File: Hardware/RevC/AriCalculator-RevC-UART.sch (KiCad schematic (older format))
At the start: 15 parts, among them CON3 USB-MINI-B, IC4 FT232RL

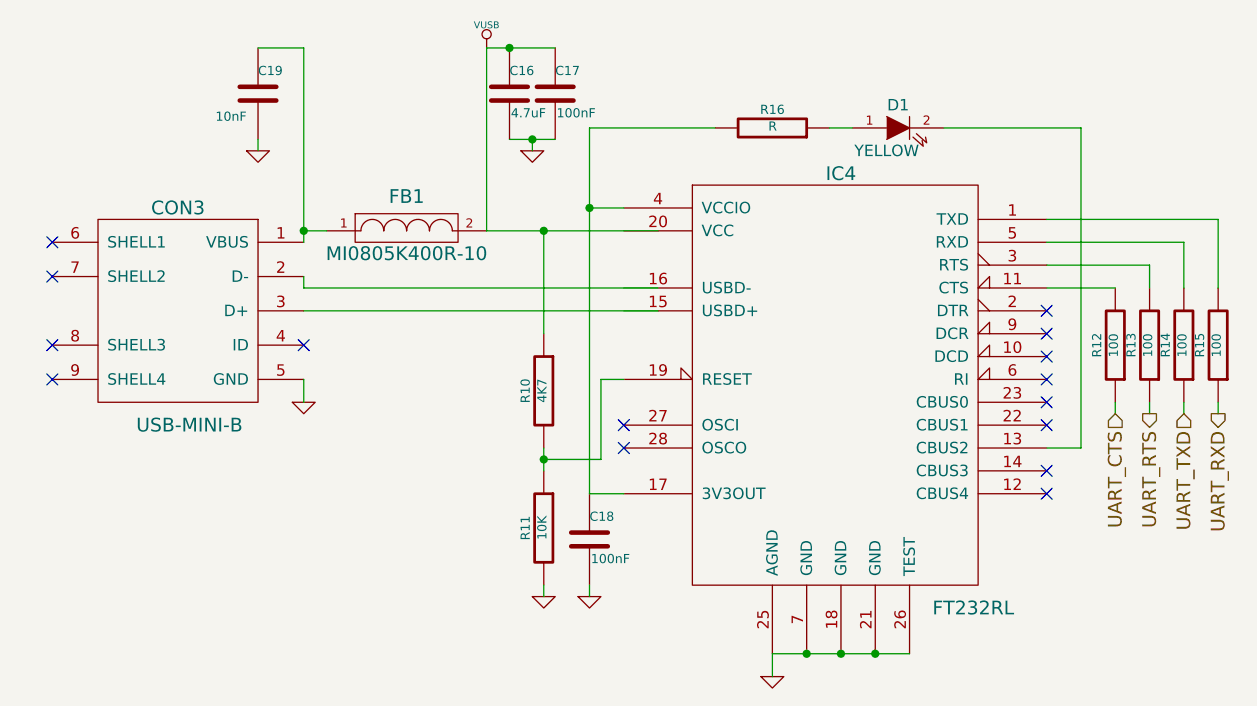
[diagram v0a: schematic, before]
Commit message: cleaned up schematic
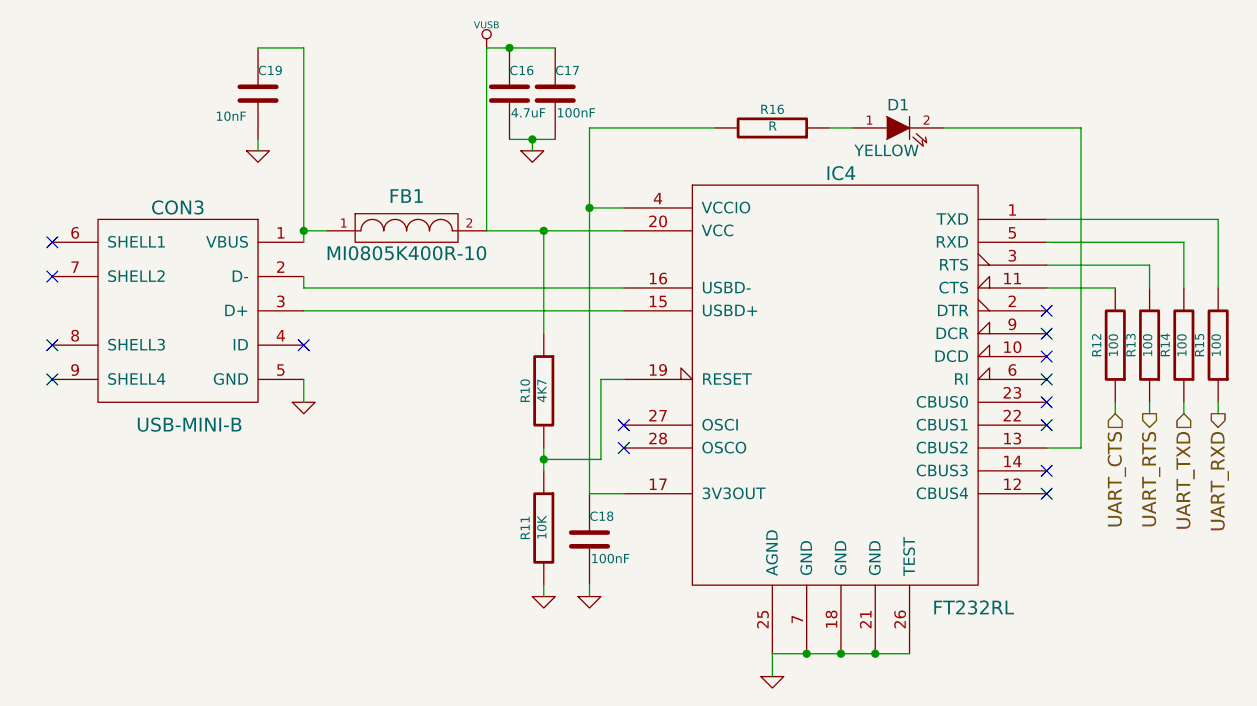
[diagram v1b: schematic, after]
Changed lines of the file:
@@
 	3650 2900 3650 3000
 Wire Wire Line
-	3400 1950 4150 1950
+	3400 1950 4000 1950
 Wire Wire Line
 	3650 1950 3650 2400
 Connection ~ 3650 2950
 Wire Wire Line
-	4150 2300 2600 2300
+	4000 2300 2600 2300
 Wire Wire Line
-	4150 2200 2600 2200
+	4000 2200 2600 2200
 Wire Wire Line
 	3850 1500 3850 3100

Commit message: work in progress
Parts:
- R16: value R -> 120
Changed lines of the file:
@@
 EESchema Schematic File Version 2
-LIBS:power
-LIBS:device
-LIBS:transistors
-LIBS:conn
-LIBS:linear
-LIBS:regul
-LIBS:74xx
-LIBS:cmos4000
-LIBS:adc-dac
-LIBS:memory
-LIBS:xilinx
-LIBS:special
-LIBS:microcontrollers
-LIBS:dsp
-LIBS:microchip
-LIBS:analog_switches
-LIBS:motorola
-LIBS:texas
-LIBS:intel
-LIBS:audio
-LIBS:interface
-LIBS:digital-audio
-LIBS:philips
-LIBS:display
-LIBS:cypress
-LIBS:siliconi
-LIBS:opto
-LIBS:atmel
-LIBS:contrib
-LIBS:valves
-LIBS:w_microcontrollers
 LIBS:AriCalculator
-LIBS:w_analog
-LIBS:w_connectors
-LIBS:w_device
-LIBS:AriCalculator-RevC-Main-cache
+LIBS:AriCalculator-RevC-cache
 EELAYER 27 0
 EELAYER END
@@
 Sheet 5 6
 Title "UART"
-Date "29 oct 2014"
+Date "3 nov 2014"
 Rev "RevC"
 Comp "Dirk Heisswolf"
@@
 P 4650 1500
 F 0 "R16" V 4730 1500 40  0000 C CNN
-F 1 "R" V 4657 1501 40  0000 C CNN
+F 1 "120" V 4657 1501 40  0000 C CNN
 F 2 "~" V 4580 1500 30  0000 C CNN
 F 3 "~" H 4650 1500 30  0000 C CNN

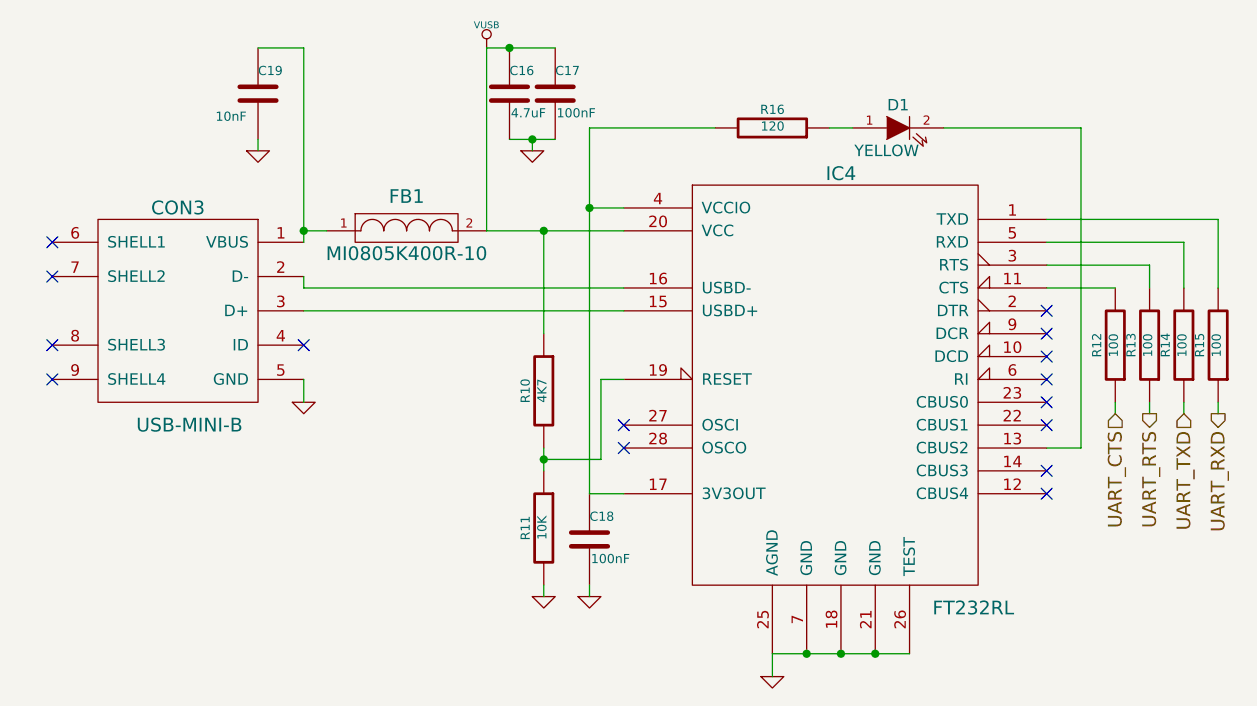
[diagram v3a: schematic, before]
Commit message: started RevC layout
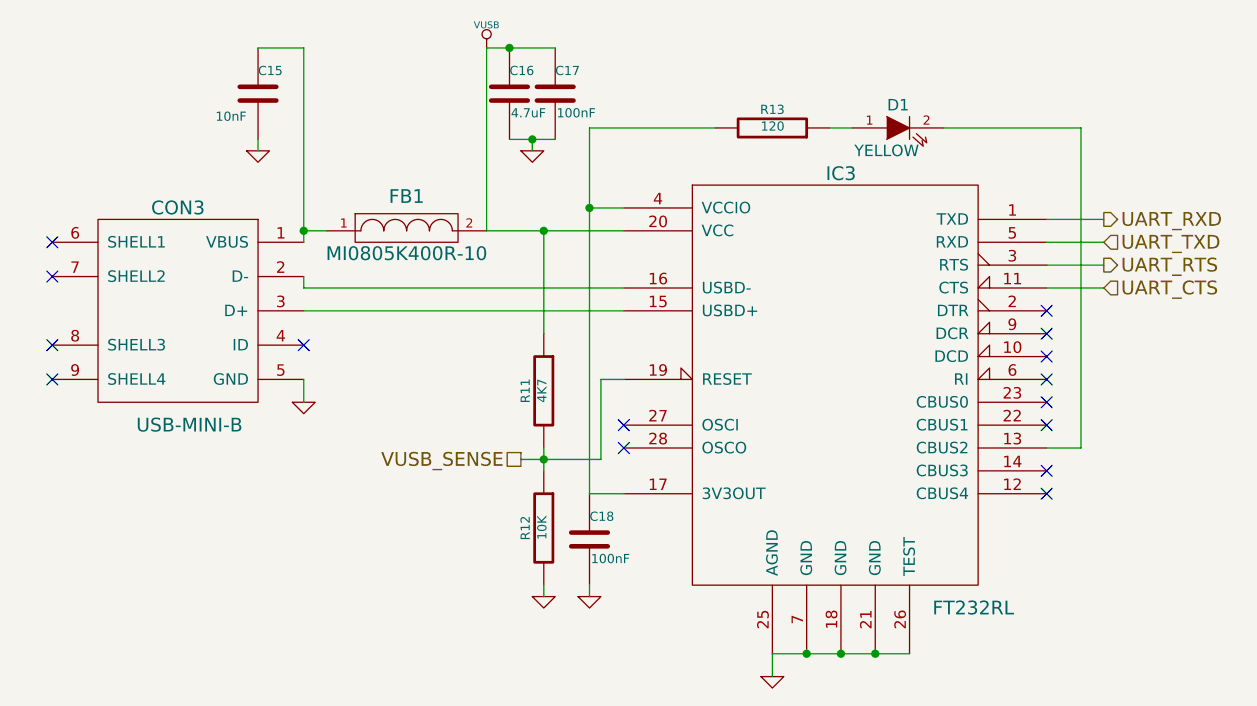
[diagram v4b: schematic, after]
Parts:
- removed R12, R13, R14, R15: 100, ~, symbol R
- renumbered C19 to C15, IC4 to IC3, R10 to R11, R11 to R12, R16 to R13
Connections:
- net UART_CTS: now also IC3.11 (CTS)
- net UART_RTS: now also IC3.3 (RTS)
- net UART_RXD: now also IC3.1 (TXD)
- net UART_TXD: now also IC3.5 (RXD)
- net VUSB_SENSE: now reaches IC3.19 (RESET), R11.2, R12.1
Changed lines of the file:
@@
 $EndDescr
 $Comp
-L FT232RL IC4
+L FT232RL IC3
 U 1 1 544AC281
 P 4950 2600
-F 0 "IC4" H 4950 3500 60  0000 C CNN
+F 0 "IC3" H 4950 3500 60  0000 C CNN
 F 1 "FT232RL" H 5350 1600 60  0000 L CNN
 F 2 "" H 4950 2600 60  0000 C CNN
@@
 	-1   0    0    -1
 $EndComp
-$Comp
-L R R12
-U 1 1 544AC3BF
-P 6150 2450
-F 0 "R12" V 6230 2450 40  0000 C CNN
-F 1 "100" V 6157 2451 40  0000 C CNN
-F 2 "~" V 6080 2450 30  0000 C CNN
-F 3 "~" H 6150 2450 30  0000 C CNN
-	1    6150 2450
-	-1   0    0    1
-$EndComp
-$Comp
-L R R13
-U 1 1 544AC3CE
-P 6300 2450
-F 0 "R13" V 6380 2450 40  0000 C CNN
-F 1 "100" V 6307 2451 40  0000 C CNN
-F 2 "~" V 6230 2450 30  0000 C CNN
-F 3 "~" H 6300 2450 30  0000 C CNN
-	1    6300 2450
-	-1   0    0    1
-$EndComp
-$Comp
-L R R14
-U 1 1 544AC3DD
-P 6450 2450
-F 0 "R14" V 6530 2450 40  0000 C CNN
-F 1 "100" V 6457 2451 40  0000 C CNN
-F 2 "~" V 6380 2450 30  0000 C CNN
-F 3 "~" H 6450 2450 30  0000 C CNN
-	1    6450 2450
-	-1   0    0    1
-$EndComp
-$Comp
-L R R15
-U 1 1 544AC3EC
-P 6600 2450
-F 0 "R15" V 6680 2450 40  0000 C CNN
-F 1 "100" V 6607 2451 40  0000 C CNN
-F 2 "~" V 6530 2450 30  0000 C CNN
-F 3 "~" H 6600 2450 30  0000 C CNN
-	1    6600 2450
-	-1   0    0    1
-$EndComp
 NoConn ~ 1500 2600
 NoConn ~ 1500 2450
@@
 NoConn ~ 4000 2800
 $Comp
-L GND #PWR017
+L GND #PWR013
 U 1 1 54502C29
 P 4650 3900
-F 0 "#PWR017" H 4650 3900 30  0001 C CNN
+F 0 "#PWR013" H 4650 3900 30  0001 C CNN
 F 1 "GND" H 4650 3830 30  0001 C CNN
 F 2 "" H 4650 3900 60  0000 C CNN
@@
 NoConn ~ 2600 2450
 $Comp
-L GND #PWR018
+L GND #PWR014
 U 1 1 54502C47
 P 2600 2700
-F 0 "#PWR018" H 2600 2700 30  0001 C CNN
+F 0 "#PWR014" H 2600 2700 30  0001 C CNN
 F 1 "GND" H 2600 2630 30  0001 C CNN
 F 2 "" H 2600 2700 60  0000 C CNN
@@
 $EndComp
 $Comp
-L GND #PWR019
+L GND #PWR015
 U 1 1 54502C84
 P 3850 3550
-F 0 "#PWR019" H 3850 3550 30  0001 C CNN
+F 0 "#PWR015" H 3850 3550 30  0001 C CNN
 F 1 "GND" H 3850 3480 30  0001 C CNN
 F 2 "" H 3850 3550 60  0000 C CNN
@@
 $EndComp
 $Comp
-L R R10
+L R R11
 U 1 1 54503F24
 P 3650 2650
-F 0 "R10" V 3730 2650 40  0000 C CNN
+F 0 "R11" V 3730 2650 40  0000 C CNN
 F 1 "4K7" V 3657 2651 40  0000 C CNN
 F 2 "~" V 3580 2650 30  0000 C CNN
@@
 $EndComp
 $Comp
-L R R11
+L R R12
 U 1 1 54503F33
 P 3650 3250
-F 0 "R11" V 3730 3250 40  0000 C CNN
+F 0 "R12" V 3730 3250 40  0000 C CNN
 F 1 "10K" V 3657 3251 40  0000 C CNN
 F 2 "~" V 3580 3250 30  0000 C CNN
@@
 $EndComp
 $Comp
-L GND #PWR020
+L GND #PWR016
 U 1 1 54503FB1
 P 3650 3550
-F 0 "#PWR020" H 3650 3550 30  0001 C CNN
+F 0 "#PWR016" H 3650 3550 30  0001 C CNN
 F 1 "GND" H 3650 3480 30  0001 C CNN
 F 2 "" H 3650 3550 60  0000 C CNN
@@
 $EndComp
 $Comp
-L R R16
+L R R13
 U 1 1 54504202
 P 4650 1500
-F 0 "R16" V 4730 1500 40  0000 C CNN
+F 0 "R13" V 4730 1500 40  0000 C CNN
 F 1 "120" V 4657 1501 40  0000 C CNN
 F 2 "~" V 4580 1500 30  0000 C CNN
@@
 $EndComp
 $Comp
-L C C19
+L C C15
 U 1 1 545042A7
 P 2400 1350
-F 0 "C19" H 2400 1450 40  0000 L CNN
+F 0 "C15" H 2400 1450 40  0000 L CNN
 F 1 "10nF" H 2350 1250 40  0000 R CNN
 F 2 "~" H 2438 1200 30  0000 C CNN
@@
 $EndComp
 $Comp
-L GND #PWR021
+L GND #PWR017
 U 1 1 545043BA
 P 2400 1600
-F 0 "#PWR021" H 2400 1600 30  0001 C CNN
+F 0 "#PWR017" H 2400 1600 30  0001 C CNN
 F 1 "GND" H 2400 1530 30  0001 C CNN
 F 2 "" H 2400 1600 60  0000 C CNN
@@
 $EndComp
 $Comp
-L GND #PWR022
+L GND #PWR018
 U 1 1 545043C9
 P 3600 1600
-F 0 "#PWR022" H 3600 1600 30  0001 C CNN
+F 0 "#PWR018" H 3600 1600 30  0001 C CNN
 F 1 "GND" H 3600 1530 30  0001 C CNN
 F 2 "" H 3600 1600 60  0000 C CNN
@@
 $EndComp
 $Comp
-L VUSB #PWR023
+L VUSB #PWR019
 U 1 1 54504942
 P 3400 1150
-F 0 "#PWR023" H 3400 1100 20  0001 C CNN
+F 0 "#PWR019" H 3400 1100 20  0001 C CNN
 F 1 "VUSB" H 3400 1250 30  0000 C CNN
 F 2 "" H 3400 1150 60  0000 C CNN
@@
 	3900 2600 3900 2950
 Wire Wire Line
-	3900 2950 3650 2950
+	3900 2950 3550 2950
 Wire Wire Line
 	2600 2200 2600 2150
@@
 Connection ~ 3650 1950
 Wire Wire Line
-	5850 2200 6150 2200
-Wire Wire Line
-	5850 2100 6300 2100
-Wire Wire Line
-	6300 2100 6300 2200
-Wire Wire Line
-	5850 2000 6450 2000
-Wire Wire Line
-	6450 2000 6450 2200
-Wire Wire Line
-	5850 1900 6600 1900
-Wire Wire Line
-	6600 1900 6600 2200
-Wire Wire Line
 	5850 2900 6000 2900
 Connection ~ 3850 1850
@@
 Wire Wire Line
 	4400 1500 3850 1500
-Text HLabel 6150 2750 3    60   Input ~ 0
+Text HLabel 6100 2200 2    60   Input ~ 0
 UART_CTS
-Text HLabel 6300 2750 3    60   Output ~ 0
+Text HLabel 6100 2100 2    60   Output ~ 0
 UART_RTS
-Text HLabel 6600 2750 3    60   Output ~ 0
+Text HLabel 6100 1900 2    60   Output ~ 0
 UART_RXD
-Text HLabel 6450 2750 3    60   Input ~ 0
+Text HLabel 6100 2000 2    60   Input ~ 0
 UART_TXD
 Wire Wire Line
-	6150 2700 6150 2750
-Wire Wire Line
-	6300 2700 6300 2750
-Wire Wire Line
-	6450 2700 6450 2750
-Wire Wire Line
-	6600 2700 6600 2750
+	6100 1900 5850 1900
+Wire Wire Line
+	6100 2000 5850 2000
+Wire Wire Line
+	6100 2100 5850 2100
+Wire Wire Line
+	6100 2200 5850 2200
+Text HLabel 3550 2950 0    60   UnSpc ~ 0
+VUSB_SENSE
 $EndSCHEMATC

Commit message: work in progress
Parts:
- renumbered D1 to LED3
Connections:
- net USBD+: now reaches CON3.3 (D+), IC3.15 (USBD+)
- net USBD-: now reaches CON3.2 (D-), IC3.16 (USBD-)
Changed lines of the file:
@@
 Sheet 5 6
 Title "UART"
-Date "5 nov 2014"
+Date "11 nov 2014"
 Rev "RevC"
 Comp "Dirk Heisswolf"
@@
 	-1   0    0    -1
 $EndComp
-NoConn ~ 1500 2600
-NoConn ~ 1500 2450
-NoConn ~ 1500 2150
-NoConn ~ 1500 2000
 NoConn ~ 4000 2900
 NoConn ~ 4000 2800
 $Comp
-L GND #PWR013
+L GND #PWR018
 U 1 1 54502C29
 P 4650 3900
-F 0 "#PWR013" H 4650 3900 30  0001 C CNN
+F 0 "#PWR018" H 4650 3900 30  0001 C CNN
 F 1 "GND" H 4650 3830 30  0001 C CNN
 F 2 "" H 4650 3900 60  0000 C CNN
@@
 NoConn ~ 2600 2450
 $Comp
-L GND #PWR014
+L GND #PWR019
 U 1 1 54502C47
 P 2600 2700
-F 0 "#PWR014" H 2600 2700 30  0001 C CNN
+F 0 "#PWR019" H 2600 2700 30  0001 C CNN
 F 1 "GND" H 2600 2630 30  0001 C CNN
 F 2 "" H 2600 2700 60  0000 C CNN
@@
 $EndComp
 $Comp
-L GND #PWR015
+L GND #PWR020
 U 1 1 54502C84
 P 3850 3550
-F 0 "#PWR015" H 3850 3550 30  0001 C CNN
+F 0 "#PWR020" H 3850 3550 30  0001 C CNN
 F 1 "GND" H 3850 3480 30  0001 C CNN
 F 2 "" H 3850 3550 60  0000 C CNN
@@
 $EndComp
 $Comp
-L GND #PWR016
+L GND #PWR021
 U 1 1 54503FB1
 P 3650 3550
-F 0 "#PWR016" H 3650 3550 30  0001 C CNN
+F 0 "#PWR021" H 3650 3550 30  0001 C CNN
 F 1 "GND" H 3650 3480 30  0001 C CNN
 F 2 "" H 3650 3550 60  0000 C CNN
@@
 $EndComp
 $Comp
-L LED D1
+L LED LED3
 U 1 1 54504211
 P 5200 1500
-F 0 "D1" H 5200 1600 50  0000 C CNN
+F 0 "LED3" H 5200 1600 50  0000 C CNN
 F 1 "YELLOW" H 5150 1400 50  0000 C CNN
 F 2 "~" H 5200 1500 60  0000 C CNN
@@
 $EndComp
 $Comp
-L GND #PWR017
+L GND #PWR022
 U 1 1 545043BA
 P 2400 1600
-F 0 "#PWR017" H 2400 1600 30  0001 C CNN
+F 0 "#PWR022" H 2400 1600 30  0001 C CNN
 F 1 "GND" H 2400 1530 30  0001 C CNN
 F 2 "" H 2400 1600 60  0000 C CNN
@@
 $EndComp
 $Comp
-L GND #PWR018
+L GND #PWR023
 U 1 1 545043C9
 P 3600 1600
-F 0 "#PWR018" H 3600 1600 30  0001 C CNN
+F 0 "#PWR023" H 3600 1600 30  0001 C CNN
 F 1 "GND" H 3600 1530 30  0001 C CNN
 F 2 "" H 3600 1600 60  0000 C CNN
@@
 $EndComp
 $Comp
-L VUSB #PWR019
+L VUSB #PWR024
 U 1 1 54504942
 P 3400 1150
-F 0 "#PWR019" H 3400 1100 20  0001 C CNN
+F 0 "#PWR024" H 3400 1100 20  0001 C CNN
 F 1 "VUSB" H 3400 1250 30  0000 C CNN
 F 2 "" H 3400 1150 60  0000 C CNN
@@
 Text HLabel 3550 2950 0    60   UnSpc ~ 0
 VUSB_SENSE
+Text Label 2650 2300 0    60   ~ 0
+USBD+
+Text Label 2650 2200 0    60   ~ 0
+USBD-
+NoConn ~ 1500 2000
+NoConn ~ 1500 2150
+NoConn ~ 1500 2450
+NoConn ~ 1500 2600
 $EndSCHEMATC

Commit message: work in progress
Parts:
- added NC? (x4): NC, symbol NC
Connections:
- net at CON3.6 (SHELL1): now also NC?.~
- net at CON3.7 (SHELL2): now also NC?.~
- net at CON3.8 (SHELL3): now also NC?.~
- net at CON3.9 (SHELL4): now also NC?.~
- no-connect marks 15 -> 11
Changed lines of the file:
@@
 Sheet 5 6
 Title "UART"
-Date "11 nov 2014"
+Date "12 nov 2014"
 Rev "RevC"
 Comp "Dirk Heisswolf"
@@
 Text Label 2650 2200 0    60   ~ 0
 USBD-
-NoConn ~ 1500 2000
-NoConn ~ 1500 2150
-NoConn ~ 1500 2450
-NoConn ~ 1500 2600
+$Comp
+L NC NC?
+U 1 1 54631CDD
+P 1450 2000
+F 0 "NC?" H 1300 1950 20  0001 C CNN
+F 1 "NC" H 1300 2050 20  0001 C CNN
+F 2 "" H 1300 1600 60  0000 C CNN
+F 3 "" H 1300 1600 60  0000 C CNN
+	1    1450 2000
+	1    0    0    -1
+$EndComp
+$Comp
+L NC NC?
+U 1 1 54631CF7
+P 1450 2150
+F 0 "NC?" H 1300 2100 20  0001 C CNN
+F 1 "NC" H 1300 2200 20  0001 C CNN
+F 2 "" H 1300 1750 60  0000 C CNN
+F 3 "" H 1300 1750 60  0000 C CNN
+	1    1450 2150
+	1    0    0    -1
+$EndComp
+$Comp
+L NC NC?
+U 1 1 54631D07
+P 1450 2450
+F 0 "NC?" H 1300 2400 20  0001 C CNN
+F 1 "NC" H 1300 2500 20  0001 C CNN
+F 2 "" H 1300 2050 60  0000 C CNN
+F 3 "" H 1300 2050 60  0000 C CNN
+	1    1450 2450
+	1    0    0    -1
+$EndComp
+$Comp
+L NC NC?
+U 1 1 54631D16
+P 1450 2600
+F 0 "NC?" H 1300 2550 20  0001 C CNN
+F 1 "NC" H 1300 2650 20  0001 C CNN
+F 2 "" H 1300 2200 60  0000 C CNN
+F 3 "" H 1300 2200 60  0000 C CNN
+	1    1450 2600
+	1    0    0    -1
+$EndComp
+Wire Wire Line
+	1500 2000 1450 2000
+Wire Wire Line
+	1500 2150 1450 2150
+Wire Wire Line
+	1500 2450 1450 2450
+Wire Wire Line
+	1500 2600 1450 2600
 $EndSCHEMATC

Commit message: work in progress
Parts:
- gave numbers to parts that had none: 4
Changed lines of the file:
@@
 Sheet 5 6
 Title "UART"
-Date "12 nov 2014"
+Date "15 nov 2014"
 Rev "RevC"
 Comp "Dirk Heisswolf"
@@
 NoConn ~ 4000 2800
 $Comp
-L GND #PWR018
+L GND #PWR26
 U 1 1 54502C29
 P 4650 3900
-F 0 "#PWR018" H 4650 3900 30  0001 C CNN
+F 0 "#PWR26" H 4650 3900 30  0001 C CNN
 F 1 "GND" H 4650 3830 30  0001 C CNN
 F 2 "" H 4650 3900 60  0000 C CNN
@@
 NoConn ~ 2600 2450
 $Comp
-L GND #PWR019
+L GND #PWR21
 U 1 1 54502C47
 P 2600 2700
-F 0 "#PWR019" H 2600 2700 30  0001 C CNN
+F 0 "#PWR21" H 2600 2700 30  0001 C CNN
 F 1 "GND" H 2600 2630 30  0001 C CNN
 F 2 "" H 2600 2700 60  0000 C CNN
@@
 $EndComp
 $Comp
-L GND #PWR020
+L GND #PWR25
 U 1 1 54502C84
 P 3850 3550
-F 0 "#PWR020" H 3850 3550 30  0001 C CNN
+F 0 "#PWR25" H 3850 3550 30  0001 C CNN
 F 1 "GND" H 3850 3480 30  0001 C CNN
 F 2 "" H 3850 3550 60  0000 C CNN
@@
 $EndComp
 $Comp
-L GND #PWR021
+L GND #PWR24
 U 1 1 54503FB1
 P 3650 3550
-F 0 "#PWR021" H 3650 3550 30  0001 C CNN
+F 0 "#PWR24" H 3650 3550 30  0001 C CNN
 F 1 "GND" H 3650 3480 30  0001 C CNN
 F 2 "" H 3650 3550 60  0000 C CNN
@@
 $EndComp
 $Comp
-L GND #PWR022
+L GND #PWR20
 U 1 1 545043BA
 P 2400 1600
-F 0 "#PWR022" H 2400 1600 30  0001 C CNN
+F 0 "#PWR20" H 2400 1600 30  0001 C CNN
 F 1 "GND" H 2400 1530 30  0001 C CNN
 F 2 "" H 2400 1600 60  0000 C CNN
@@
 $EndComp
 $Comp
-L GND #PWR023
+L GND #PWR23
 U 1 1 545043C9
 P 3600 1600
-F 0 "#PWR023" H 3600 1600 30  0001 C CNN
+F 0 "#PWR23" H 3600 1600 30  0001 C CNN
 F 1 "GND" H 3600 1530 30  0001 C CNN
 F 2 "" H 3600 1600 60  0000 C CNN
@@
 $EndComp
 $Comp
-L VUSB #PWR024
+L VUSB #PWR22
 U 1 1 54504942
 P 3400 1150
-F 0 "#PWR024" H 3400 1100 20  0001 C CNN
+F 0 "#PWR22" H 3400 1100 20  0001 C CNN
 F 1 "VUSB" H 3400 1250 30  0000 C CNN
 F 2 "" H 3400 1150 60  0000 C CNN
@@
 USBD-
 $Comp
-L NC NC?
+L NC NC1
 U 1 1 54631CDD
 P 1450 2000
-F 0 "NC?" H 1300 1950 20  0001 C CNN
+F 0 "NC1" H 1300 1950 20  0001 C CNN
 F 1 "NC" H 1300 2050 20  0001 C CNN
 F 2 "" H 1300 1600 60  0000 C CNN
@@
 $EndComp
 $Comp
-L NC NC?
+L NC NC2
 U 1 1 54631CF7
 P 1450 2150
-F 0 "NC?" H 1300 2100 20  0001 C CNN
+F 0 "NC2" H 1300 2100 20  0001 C CNN
 F 1 "NC" H 1300 2200 20  0001 C CNN
 F 2 "" H 1300 1750 60  0000 C CNN
@@
 $EndComp
 $Comp
-L NC NC?
+L NC NC3
 U 1 1 54631D07
 P 1450 2450
-F 0 "NC?" H 1300 2400 20  0001 C CNN
+F 0 "NC3" H 1300 2400 20  0001 C CNN
 F 1 "NC" H 1300 2500 20  0001 C CNN
 F 2 "" H 1300 2050 60  0000 C CNN
@@
 $EndComp
 $Comp
-L NC NC?
+L NC NC4
 U 1 1 54631D16
 P 1450 2600
-F 0 "NC?" H 1300 2550 20  0001 C CNN
+F 0 "NC4" H 1300 2550 20  0001 C CNN
 F 1 "NC" H 1300 2650 20  0001 C CNN
 F 2 "" H 1300 2200 60  0000 C CNN
